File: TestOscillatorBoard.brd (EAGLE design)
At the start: 70.1 x 24 mm, 0 parts

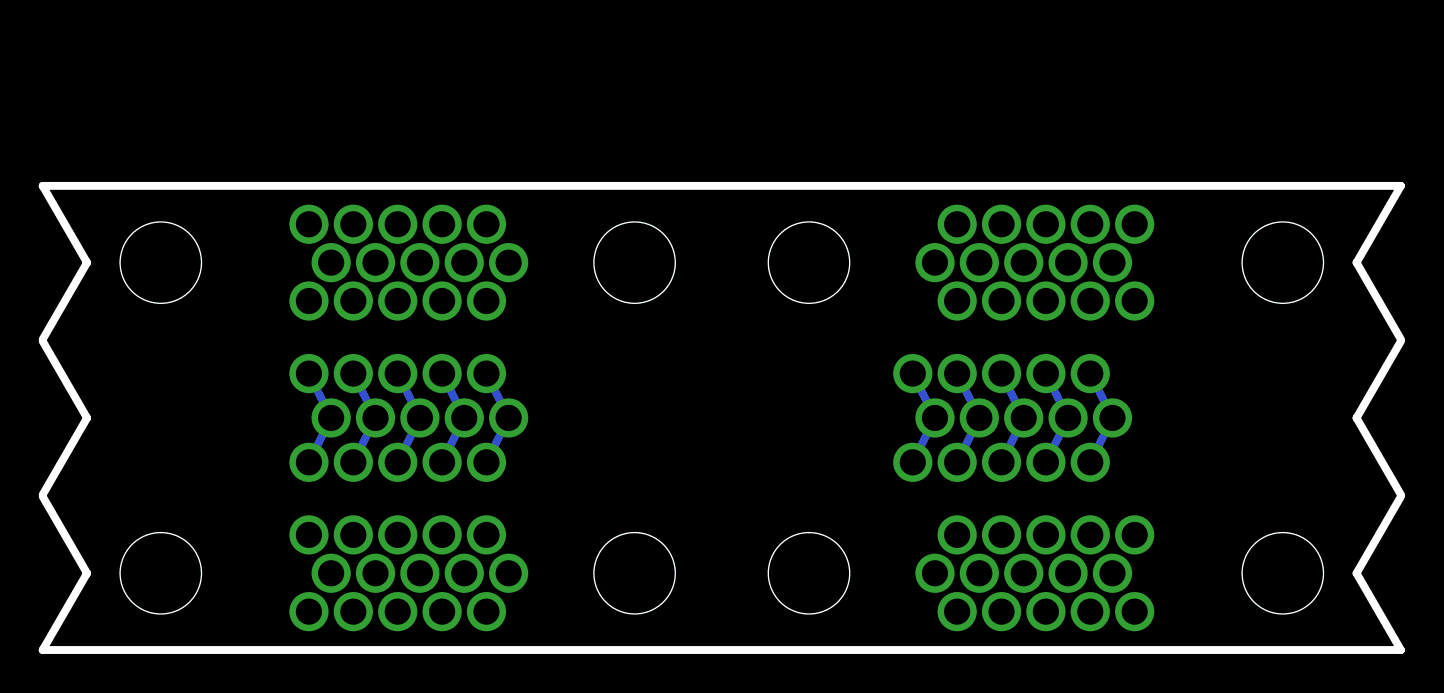
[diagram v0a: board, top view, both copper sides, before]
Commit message: Various changes to the board. With this, the testing setup has been functional for quite a while...
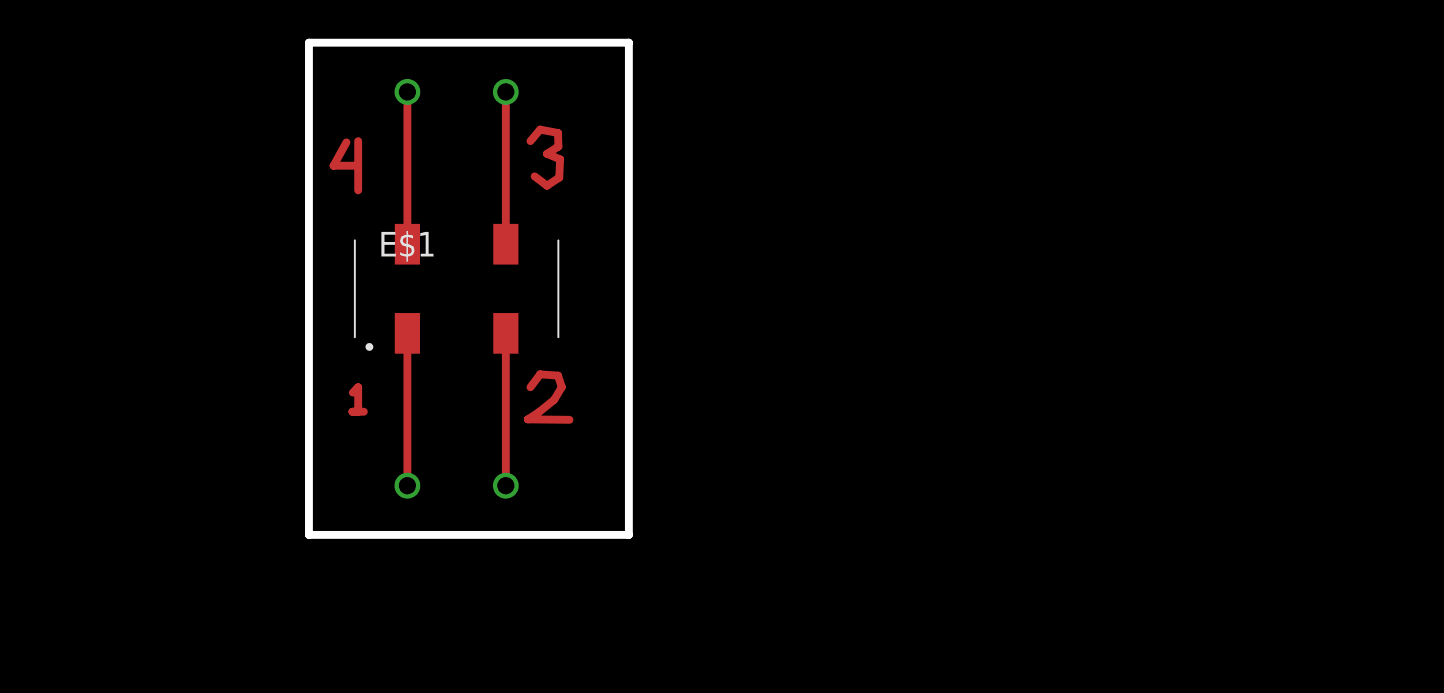
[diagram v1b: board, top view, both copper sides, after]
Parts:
- added E$1: (no value), SG-636PCW_50.0000MC3__ROHS:SG-636
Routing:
- net S$4: track 0.00 -> 7.62 mm, vias 0 -> 1
- net S$3: track 0.00 -> 7.62 mm, vias 0 -> 1
- net S$2: track 0.00 -> 7.62 mm, vias 0 -> 1
- net S$1: track 0.00 -> 7.62 mm, vias 0 -> 1
- net S$6: track 0.00 -> 6.99 mm
- net S$7: track 0.00 -> 6.36 mm
- net S$8: track 0.00 -> 5.19 mm
- net C2_17: track 5.12 -> 0.00 mm, vias 3 -> 0
- net C29: track 5.12 -> 0.00 mm, vias 3 -> 0
- net C27: track 5.12 -> 0.00 mm, vias 3 -> 0
- net C17: track 5.12 -> 0.00 mm, vias 3 -> 0
- net C30: track 5.12 -> 0.00 mm, vias 3 -> 0
- net C2_30: track 5.12 -> 0.00 mm, vias 3 -> 0
- net C28: track 5.12 -> 0.00 mm, vias 3 -> 0
- net C2_29: track 5.12 -> 0.00 mm, vias 3 -> 0
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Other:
- board size 70.1 x 24 mm -> 16.5 x 25.4 mm
